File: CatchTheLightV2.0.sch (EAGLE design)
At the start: 46 parts, among them J1 TC2030-IDC-NL, U1 ATMEGA328PB-ANR

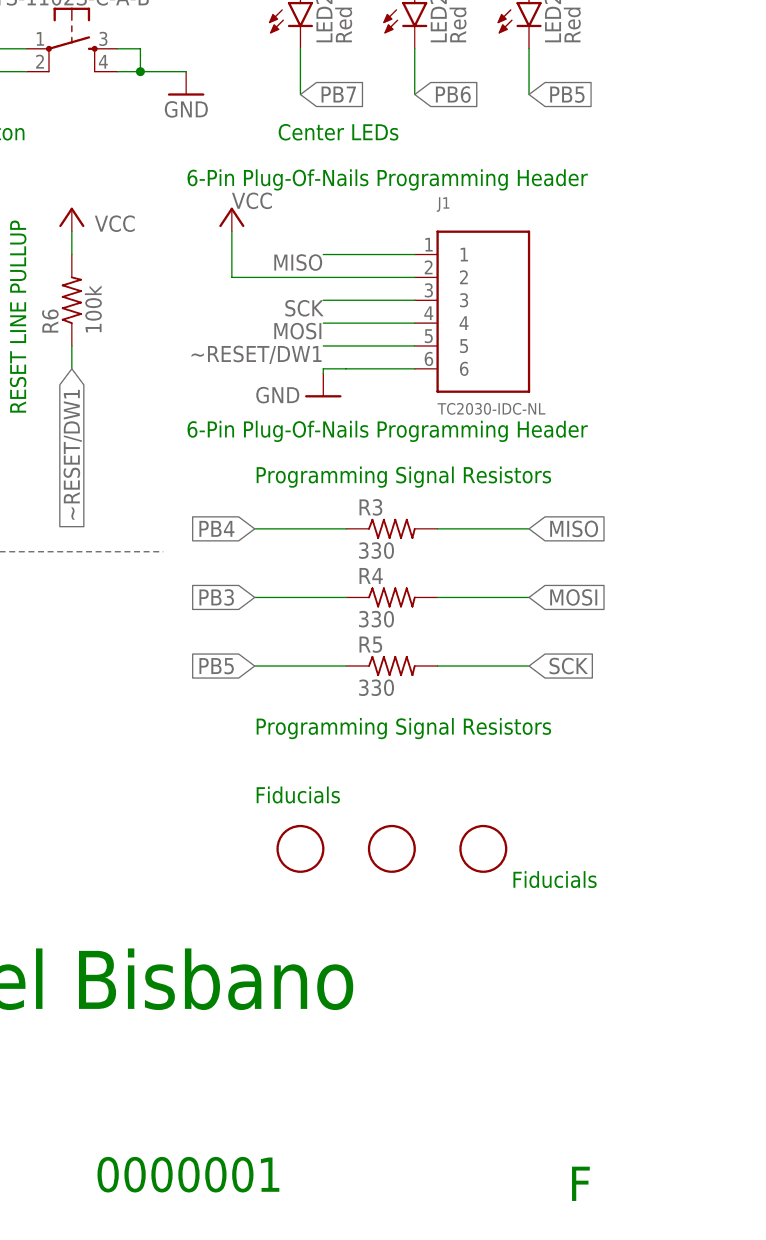
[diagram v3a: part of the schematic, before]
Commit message: Removed Programming line resistors
Removed programming line resistors and renamed plug of nails to bed of nails.
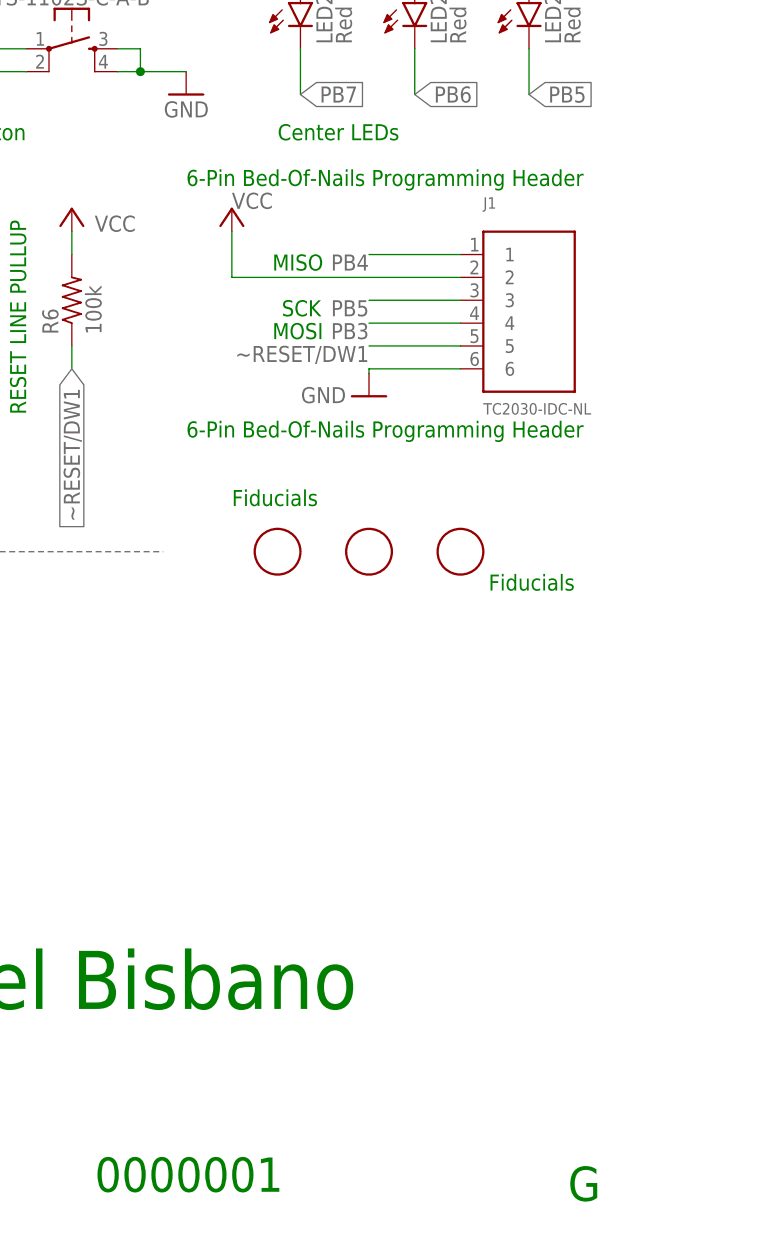
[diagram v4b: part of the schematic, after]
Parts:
- removed R3, R4, R5: 330, rcl:R-US_R0805
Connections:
- removed net MISO: J1.1, R3.2
- removed net MOSI: J1.4, R4.2
- removed net SCK: J1.3, R5.2
- net PB3: now also J1.4; no longer R4.1
- net PB4: now also J1.1; no longer R3.1
- net PB5: now also J1.3; no longer R5.1
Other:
- note added: "6-Pin Bed-Of-Nails Programming Header"
- note added: "G"
- note added: "MISO"
- note added: "MOSI"
- note added: "SCK"
- note removed: "6-Pin Plug-Of-Nails Programming Header"
- note removed: "F"
- note removed: "Programming Signal Resistors"
- moved on the sheet: J1

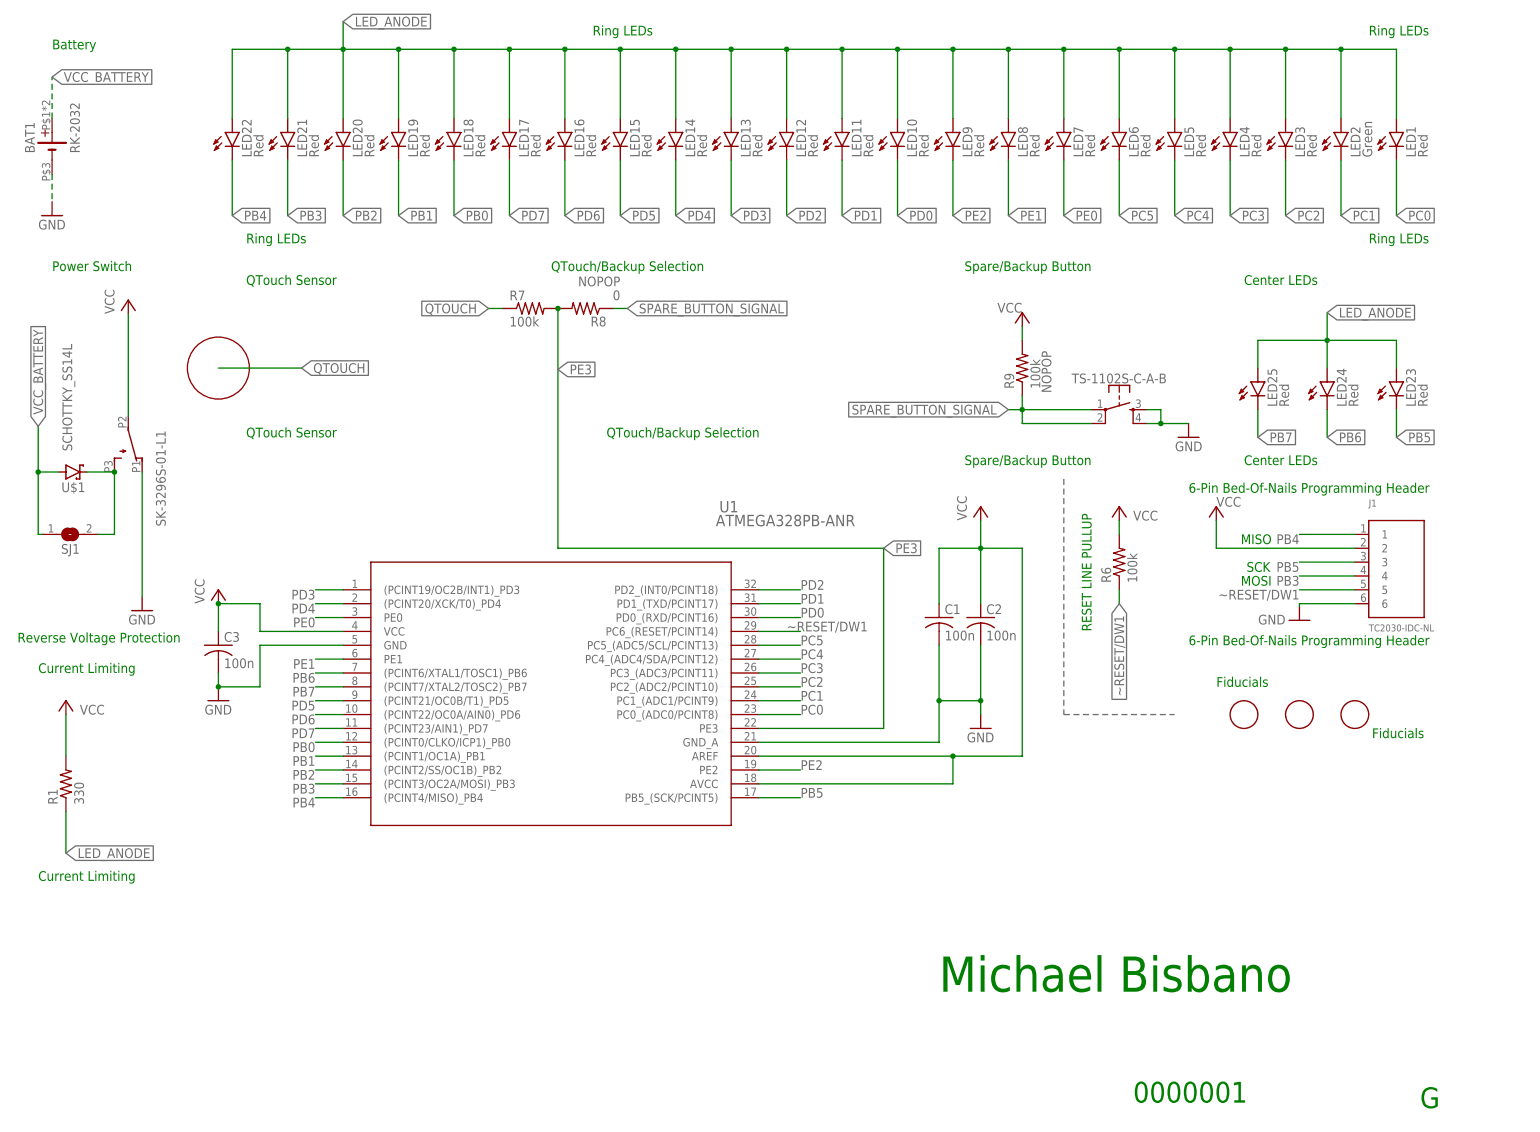
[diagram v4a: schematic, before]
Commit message: PMOS Reverse Protection in Schematic and Board
Swapped in PMOS over Schottky diode for reverse protection
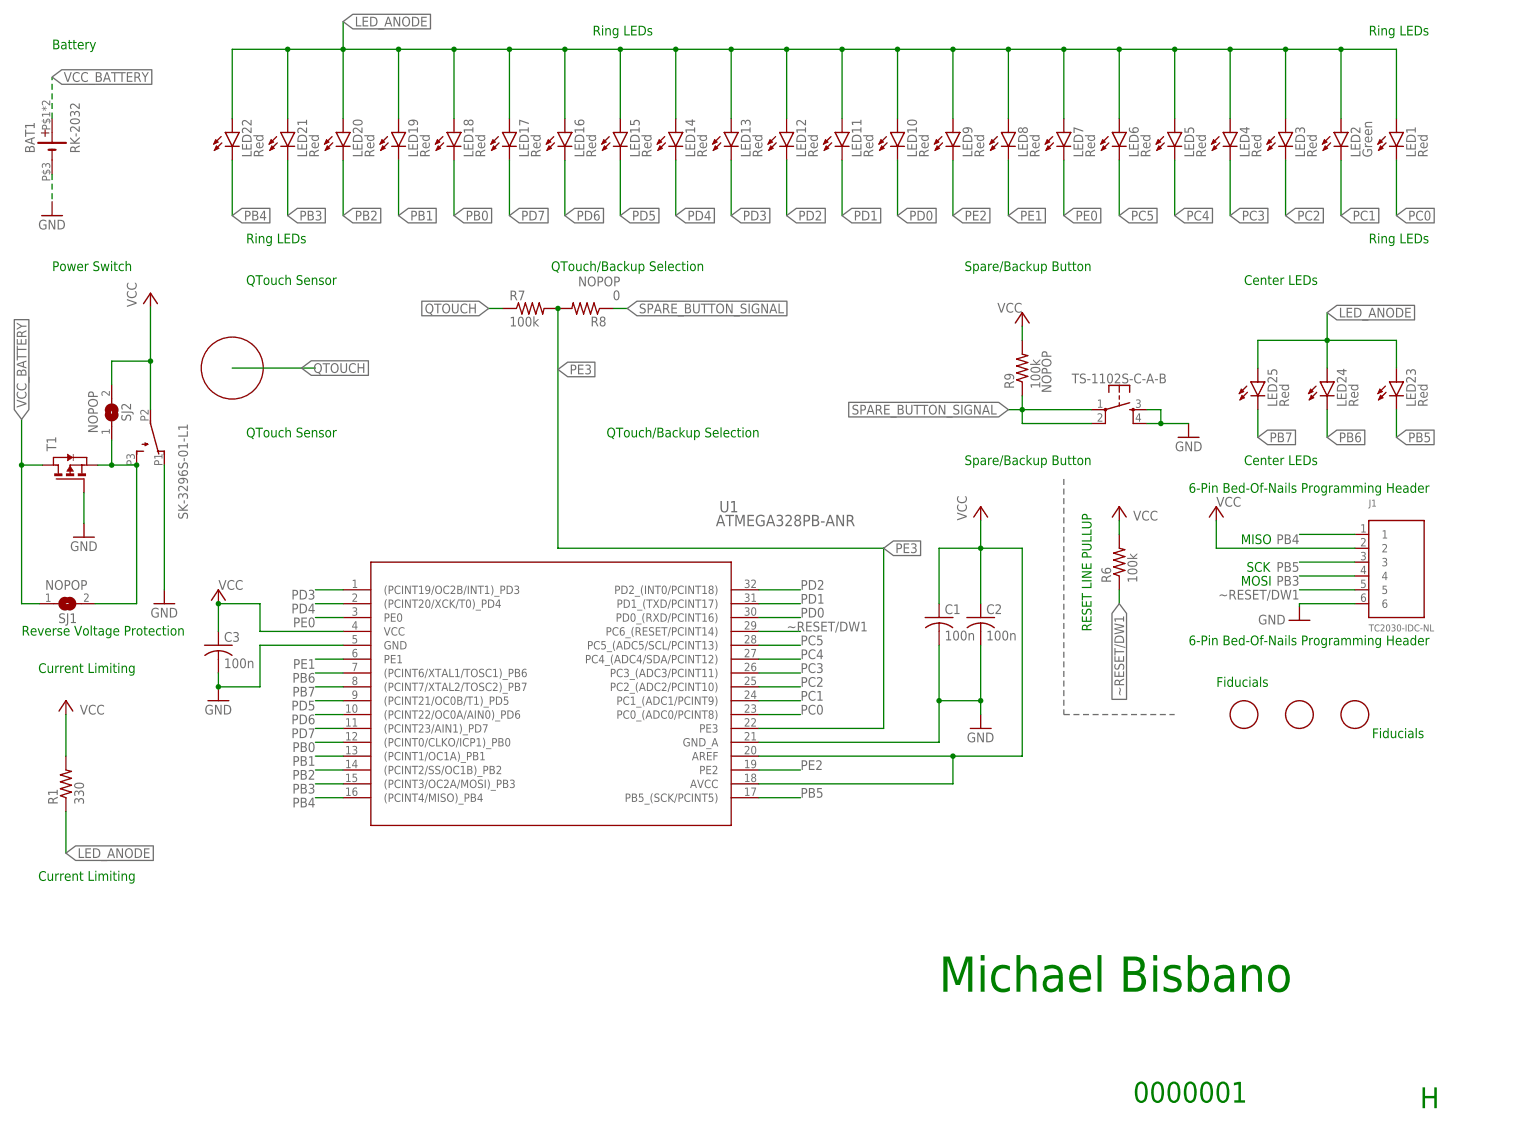
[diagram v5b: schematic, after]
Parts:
- removed U$1: SCHOTTKY_SS14L, ECE_388_CustomParts_V1.1:SCHOTTKY_SS14L
- added SJ2: NOPOP, ECE388:SJW
- added T1: (no value), zetex:PMOSSOT23
- SJ1: value (none) -> NOPOP
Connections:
- net GND: now also T1.G
- net PROTECTED_VBAT: now also SJ2.1, T1.S; no longer U$1.C
- net VCC: now also SJ2.2
- net VCC_BATTERY: now also T1.D; no longer U$1.A
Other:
- note added: "H"
- note removed: "G"
- moved on the sheet: SJ1
